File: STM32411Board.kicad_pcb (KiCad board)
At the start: 4 copper layers, 18 parts, among them J1 Conn_02x10_Odd_Even, U1 STM32F411CEUx, Y1 25Mhz 8pF, Y2 32kHz 8pF

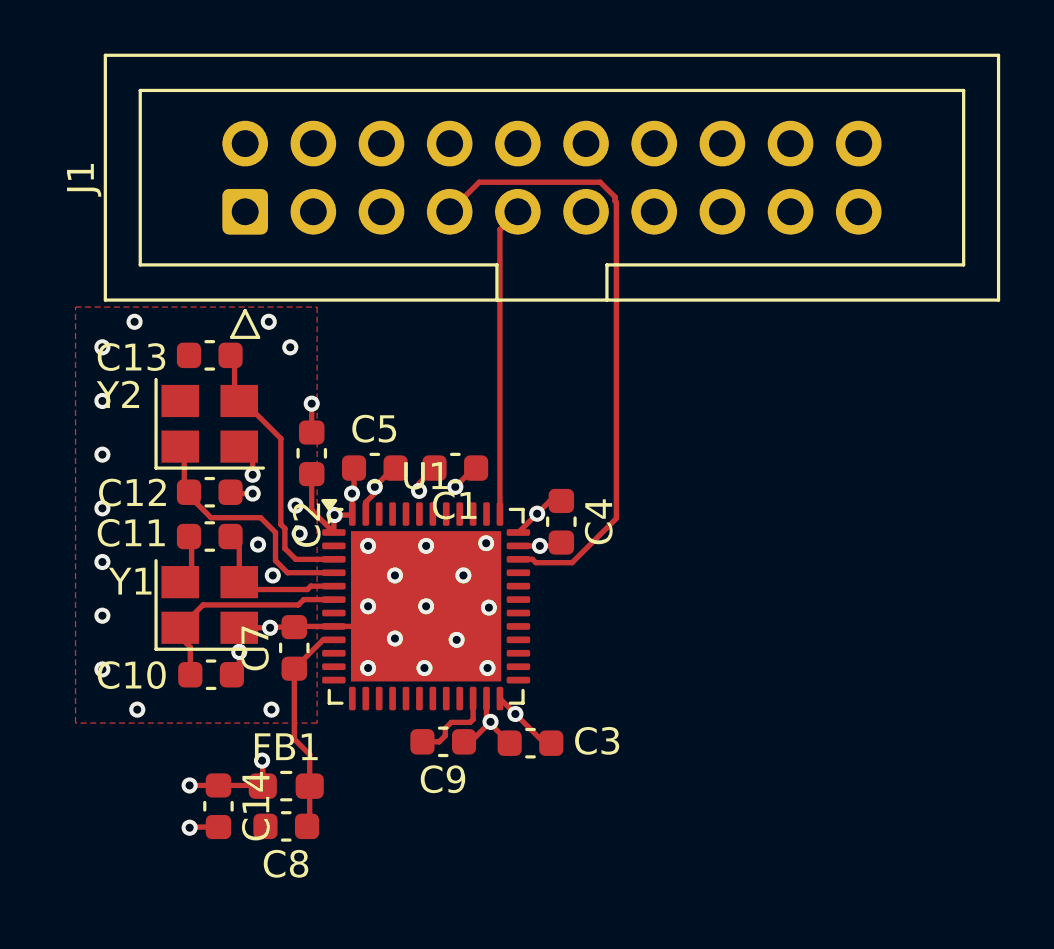
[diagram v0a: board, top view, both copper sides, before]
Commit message: updated crystal
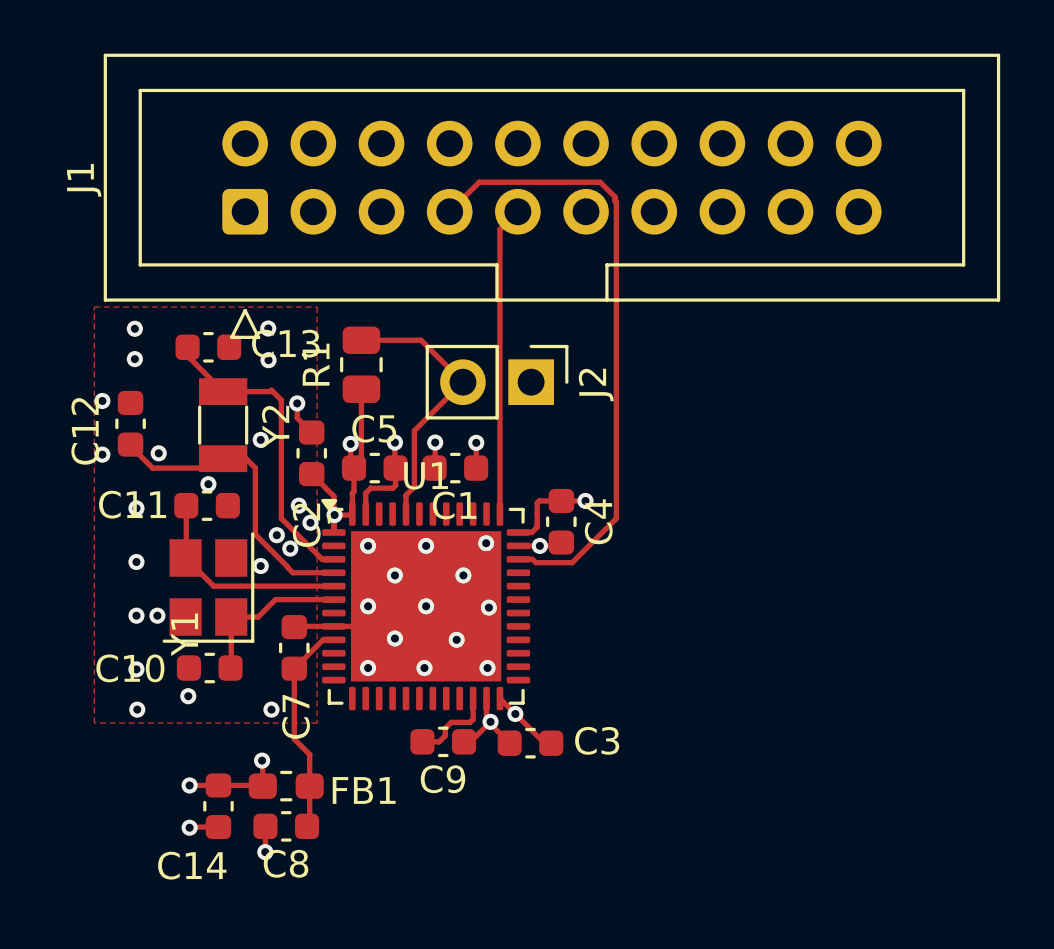
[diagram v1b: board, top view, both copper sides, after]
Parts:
- added J2: Conn_01x02, Connector_PinHeader_2.54mm:PinHeader_1x02_P2.54mm_Vertical, F.Cu at (156.0, 42.3)
- added R1: 10k, Resistor_SMD:R_0805_2012Metric, F.Cu at (149.7, 41.6)
- Y2: value 32kHz 8pF -> Crystal; footprint Crystal:Crystal_SMD_3225-4Pin_3.2x2.5mm -> Crystal:Crystal_SMD_3215-2Pin_3.2x1.5mm
- moved C12 3.90 mm to (141.1, 43.9), turned to 90 degrees
- moved C11 1.15 mm to (143.9, 46.9), turned to 0 degrees
- moved Y1 0.65 mm to (143.9, 50.0), turned to 90 degrees
- moved Y2 0.50 mm to (144.5, 43.9), turned to -90 degrees
- moved C13 0.30 mm to (143.9, 41.0), turned to 0 degrees
- moved C10 0.25 mm to (144.0, 53.0), turned to 180 degrees
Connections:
- Y2 pad 2: GND -> /osc32_in
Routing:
- net /boot0: track 0.00 -> 10.2 mm
- net +3V3: track 15.1 -> 20.4 mm
- net GND: track 22.3 -> 17.1 mm, vias 39 -> 42
- net /osc_in: track 5.43 -> 7.92 mm
- net /osc_out: track 8.35 -> 6.00 mm
- net /osc32_out: track 9.10 -> 11.3 mm
- net /osc32_in: track 10.2 -> 11.5 mm
